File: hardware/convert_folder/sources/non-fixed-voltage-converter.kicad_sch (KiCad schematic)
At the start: 11 parts

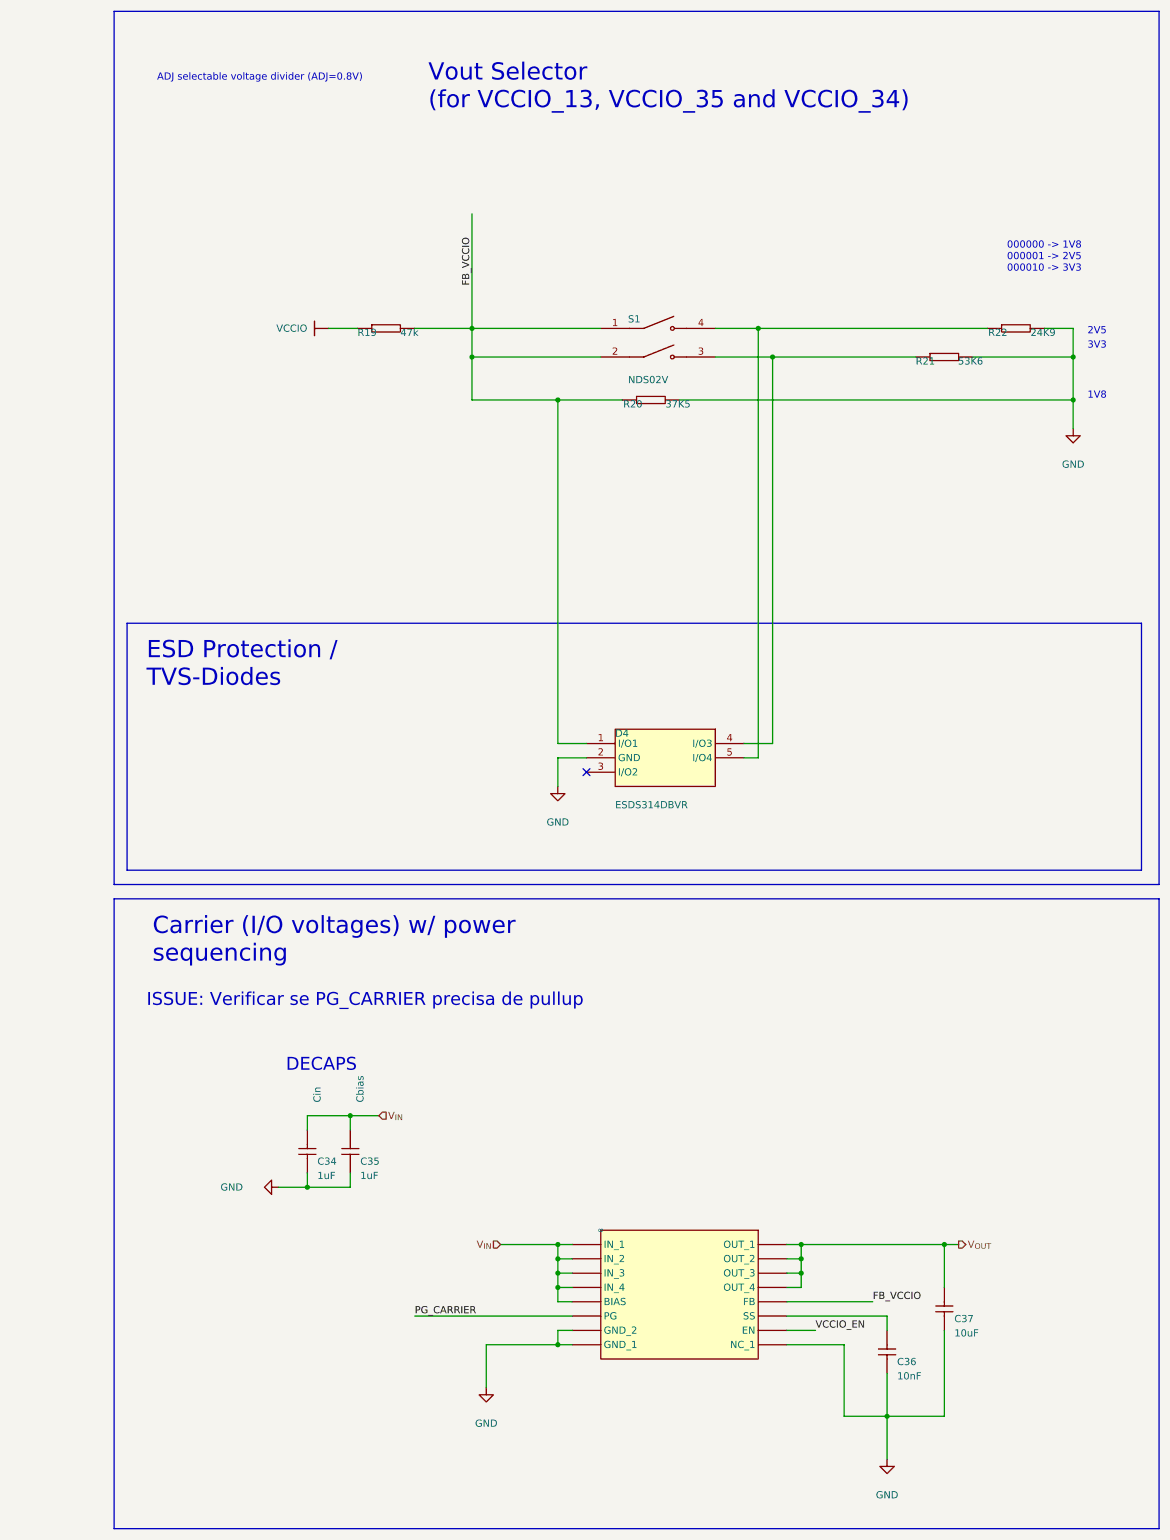
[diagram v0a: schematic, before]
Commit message: fix: start fixing the power converters of the board
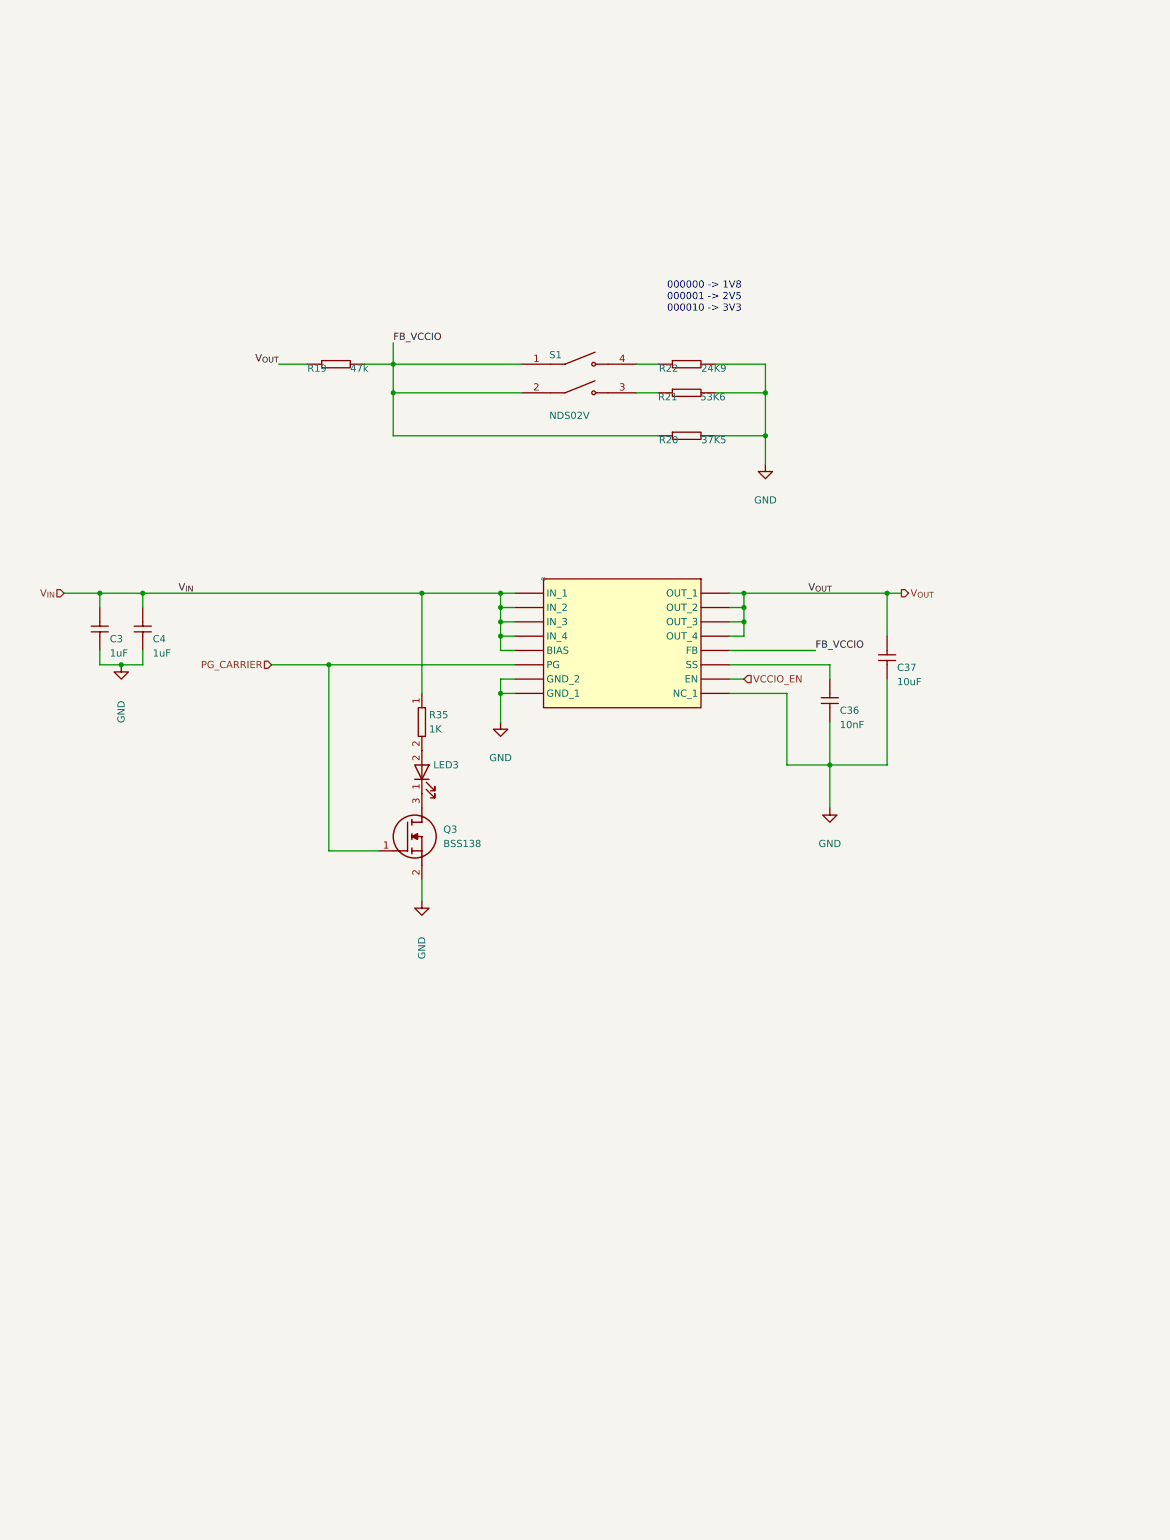
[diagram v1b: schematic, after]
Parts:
- removed C34: Cin, altium_import:C0603_MD, symbol altium_import:root_0_UMK107BJ105KA-T_Capacitor.SchLib
- removed C35: Cbias, altium_import:C0603_MD, symbol altium_import:root_0_UMK107BJ105KA-T_Capacitor.SchLib
- removed D4: ESDS314DBVR, altium_import:SOT95P280X145-5N, symbol altium_import:root_0_ESDS314DBVR_*
- added C3: Cin, altium_import:C0603_MD, symbol altium_import:root_0_UMK107BJ105KA-T_Capacitor.SchLib
- added C4: Cbias, altium_import:C0603_MD, symbol altium_import:root_0_UMK107BJ105KA-T_Capacitor.SchLib
- added LED3: LTST-C190GKT, LEDC1608X90N, symbol lib:LTST-C190GKT
- added Q3: BSS138, SOT95P240X120-3N, symbol lib:BSS138
- added R35: 1K, RESC1608X55N, symbol lib:CRCW06031K00FKEAHP
- 8: value (none) -> ~
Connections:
- net VCCIO is gone; now on net V_{OUT}: R19.1
- net GND: now also C3.2, C4.2, Q3.2 (S)
- net PG_CARRIER: now also Q3.1 (G)
- net V_{IN}: now also C3.1, C4.1, R35.1
- new net: LED3.1 (K), Q3.3 (D)
- new net: LED3.2 (A), R35.2
- no-connect marks 1 -> 0
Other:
- note removed: "1V8"
- note removed: "2V5"
- note removed: "3V3"
- note removed: "ADJ selectable voltage divider (ADJ=0.8V)"
- note removed: "DECAPS"
- moved on the sheet: 8, C36, C37, R19, R20, R21, R22, S1

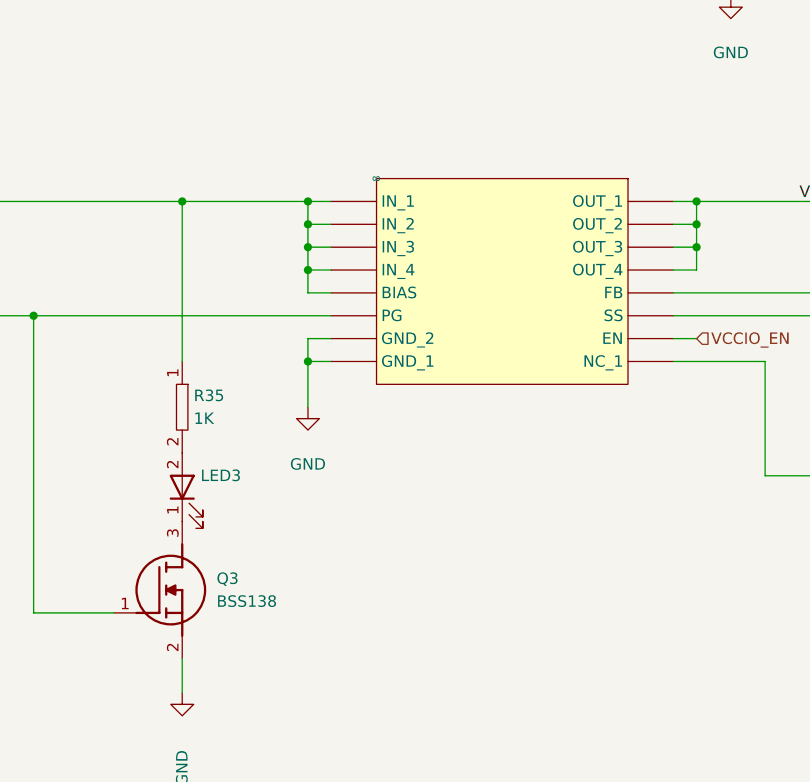
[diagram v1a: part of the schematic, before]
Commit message: fix: add more fixes to the power converters, add resets and other minor corrections
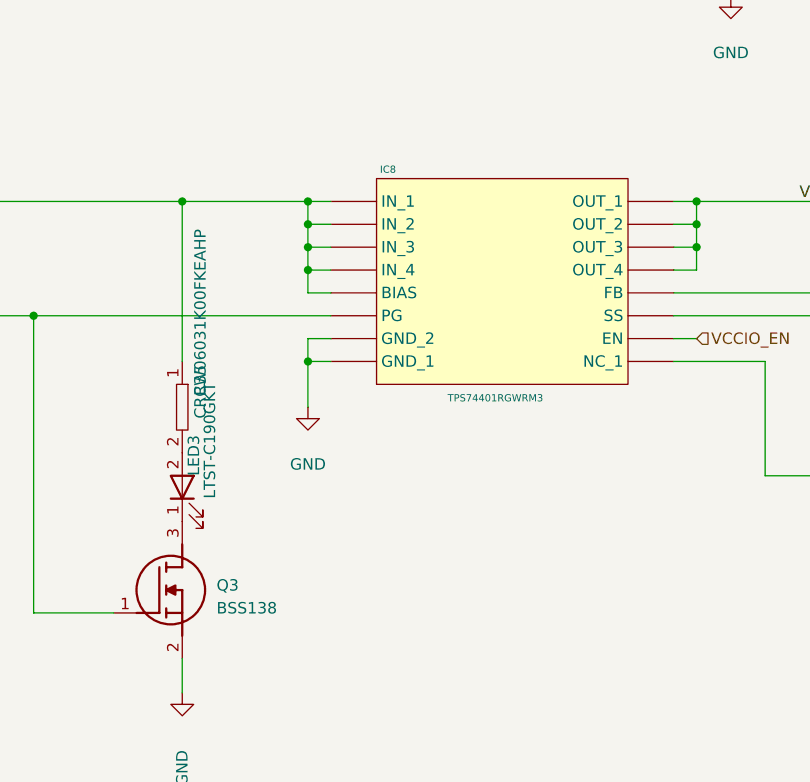
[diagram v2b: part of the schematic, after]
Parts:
- IC8: renamed from 8; value ~ -> TPS74401RGWRM3
- LED3: footprint LEDC1608X90N -> lib:LTST-C190GKT
- Q3: footprint SOT95P240X120-3N -> lib:BSS138
- R35: value 1K -> CRCW06031K00FKEAHP; footprint RESC1608X55N -> lib:CRCW06031K00FKEAHP
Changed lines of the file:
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@@
 		(on_board yes)
 		(dnp no)
-		(property "Reference" "8"
-			(at 287.02 168.91 0)
+		(property "Reference" "IC8"
+			(at 288.29 167.894 90)
 			(do_not_autoplace yes)
 			(effects
@@
 			)
 		)
-		(property "Value" "~"
-			(at 287.02 194.31 0)
+		(property "Value" "TPS74401RGWRM3"
+			(at 300.228 193.294 90)
 			(do_not_autoplace yes)
 			(effects
@@
 			(project "flatsat_platform_2"
 				(path "/8c88a7e1-4137-48d7-b926-b5e762e3852f/8386d232-e6d5-4b15-8289-83f2ee4d46fe/49e7c018-e125-40f5-b5d8-5320986f9db2"
-					(reference "8")
+					(reference "IC8")
 					(unit 1)
 				)
 				(path "/8c88a7e1-4137-48d7-b926-b5e762e3852f/8386d232-e6d5-4b15-8289-83f2ee4d46fe/93ce5ee5-515b-44f0-a5c2-2f4d8eca03ed"
-					(reference "1")
+					(reference "IC1")
 					(unit 1)
 				)
@@
 					(size 1.27 1.27)
 				)
-				(justify left)
+				(justify left top)
 			)
 		)
@@
 					(size 1.27 1.27)
 				)
-				(justify left)
-			)
-		)
-		(property "Footprint" "SOT95P240X120-3N"
+				(justify left top)
+			)
+		)
+		(property "Footprint" "lib:BSS138"
 			(at 269.24 315.9 0)
 			(effects
@@
 		(fields_autoplaced yes)
 		(property "Reference" "R35"
-			(at 266.7 193.0399 90)
-			(effects
-				(font
-					(size 1.27 1.27)
-				)
-				(justify right)
-			)
-		)
-		(property "Value" "1K"
-			(at 266.7 195.5799 90)
-			(effects
-				(font
-					(size 1.27 1.27)
-				)
-				(justify right)
-			)
-		)
-		(property "Footprint" "RESC1608X55N"
+			(at 266.7 193.0399 0)
+			(effects
+				(font
+					(size 1.27 1.27)
+				)
+				(justify left top)
+			)
+		)
+		(property "Value" "CRCW06031K00FKEAHP"
+			(at 266.7 195.5799 0)
+			(effects
+				(font
+					(size 1.27 1.27)
+				)
+				(justify left top)
+			)
+		)
+		(property "Footprint" "lib:CRCW06031K00FKEAHP"
 			(at 361.62 189.23 0)
 			(effects
@@
 		(dnp no)
 		(property "Reference" "LED3"
-			(at 267.462 201.93 90)
-			(effects
-				(font
-					(size 1.27 1.27)
-				)
-				(justify right)
+			(at 267.462 201.93 0)
+			(effects
+				(font
+					(size 1.27 1.27)
+				)
+				(justify left bottom)
 			)
 		)
 		(property "Value" "LTST-C190GKT"
-			(at 269.24 204.4699 90)
-			(effects
-				(font
-					(size 1.27 1.27)
-				)
-				(justify right)
-				(hide yes)
-			)
-		)
-		(property "Footprint" "LEDC1608X90N"
+			(at 269.24 204.4699 0)
+			(effects
+				(font
+					(size 1.27 1.27)
+				)
+				(justify left bottom)
+			)
+		)
+		(property "Footprint" "lib:LTST-C190GKT"
 			(at 359.08 198.12 0)
 			(effects

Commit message: fix: start the layout of power path
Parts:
- removed S1: NDS02V, altium_import:NDS02V, symbol altium_import:root_0_NDS02V_SamacSys.SchLib
- added J17, J7: 5-146280-2, altium_import:PIN BAR 2 2.54mm 180 GRAUS, symbol altium_import:root_0_5-146280-2_flatsat_platform_2.SchLib
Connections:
- net FB_VCCIO: now also J17.1, J7.1
- net at R21.1: now also J17.2
- net at R22.1: now also J7.2
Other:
- moved on the sheet: R20

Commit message: fix: fix caps. values, add decoupling capacitors for INAs and other ICs, and add general improvements
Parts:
- C3: value Cin -> UMK107BJ105KA-T
- C37: value Cout -> GRM188C81C106MA73D
- C4: value Cbias -> UMK107BJ105KA-T
- R20: value ERJ-H3ED3652V -> ERJ-H3ED3752V
- R21: value ERJH3ED3652V -> ERJ-H3ED5362V
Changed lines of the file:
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@@
 			)
 		)
-		(property "Value" "Cin"
+		(property "Value" "UMK107BJ105KA-T"
 			(at 204.724 177.038 90)
 			(effects
@@
 			)
 		)
-		(property "Value" "ERJH3ED3652V"
+		(property "Value" "ERJ-H3ED5362V"
 			(at 306.832 135.001 0)
 			(effects
@@
 			)
 		)
-		(property "Value" "ERJ-H3ED3652V"
+		(property "Value" "ERJ-H3ED3752V"
 			(at 309.626 150.749 0)
 			(effects
@@
 			)
 		)
-		(property "Value" "Cout"
+		(property "Value" "GRM188C81C106MA73D"
 			(at 346.202 178.562 90)
 			(effects
@@
 			)
 		)
-		(property "Value" "Cbias"
+		(property "Value" "UMK107BJ105KA-T"
 			(at 224.79 176.53 90)
 			(effects
